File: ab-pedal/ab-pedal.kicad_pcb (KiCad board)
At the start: 2 copper layers, 102.2 x 47.8 mm, 31 parts, among them J1 PEDAL, J2 IN, J4 SEND, J6 RECV, J7 OUT, J8 Jack-DC, SW1 TRUE_BYPASS, SW2 INVERT, SW3 ON, U1 TL074, U2 MAX1044, U3 LM317_TO-220, U4 LM337_TO220

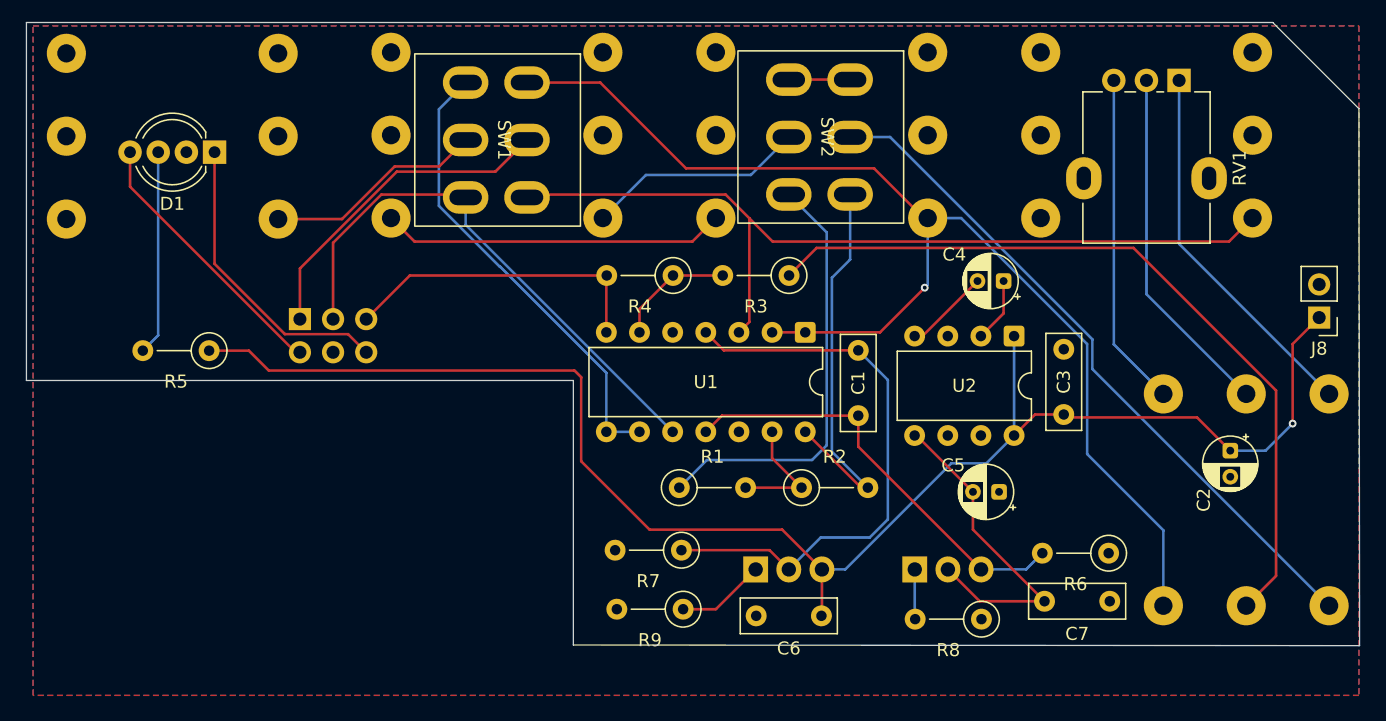
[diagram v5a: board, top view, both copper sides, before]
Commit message: sandwich in ground plane
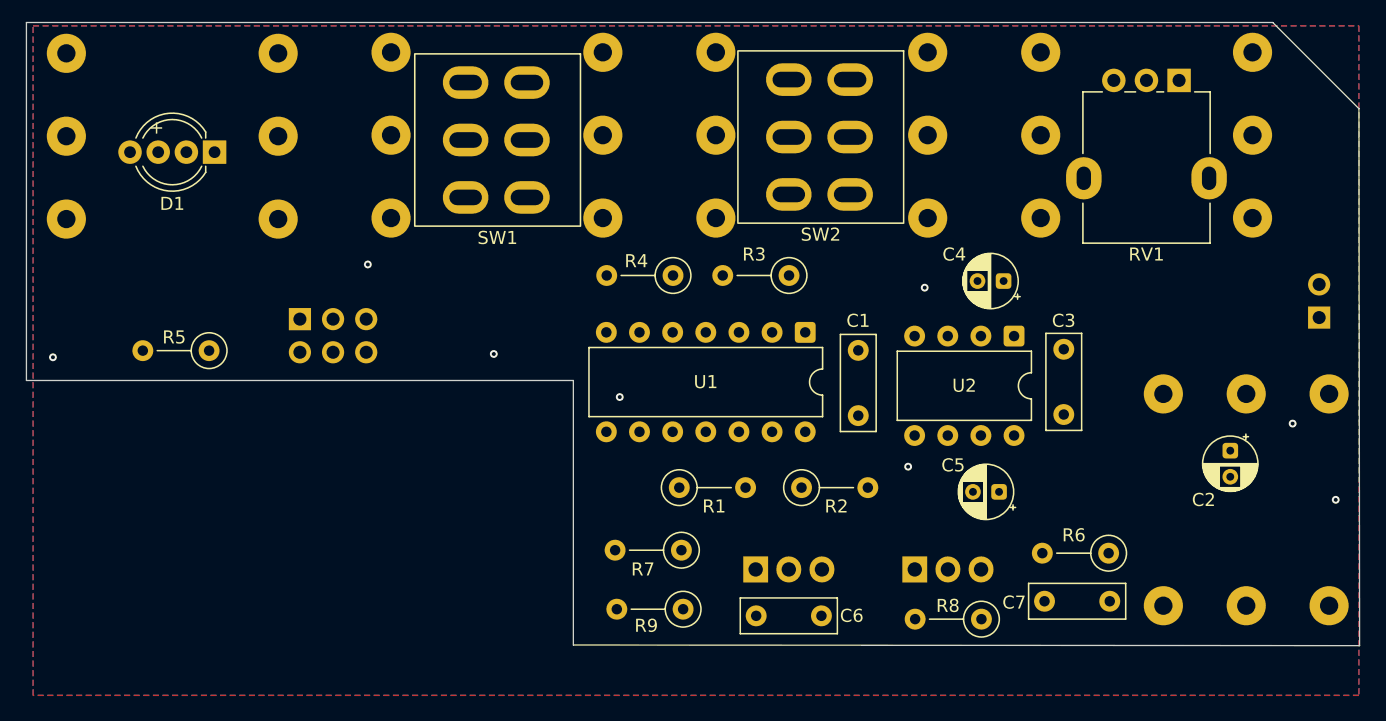
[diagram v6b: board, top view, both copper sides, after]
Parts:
- J8: moved to B.Cu
- turned J8 to 0 degrees
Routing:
- net GND: vias 0 -> 6
- added copper zone on In1.Cu, net GND
- added copper zone on In2.Cu, net GND
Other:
- copper layers 2 -> 4
- board text added: "+"
- board text added: "AB-SW Rev A 2026-07-20"
- board text added: "EXP"
- board text added: "IN"
- board text added: "OUT"
- board text added: "RECV"
- board text added: "SEND"
- board text added: "STOMPSW"
